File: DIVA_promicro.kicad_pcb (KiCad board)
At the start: 2 copper layers, 65.8 x 91.4 mm, 25 parts

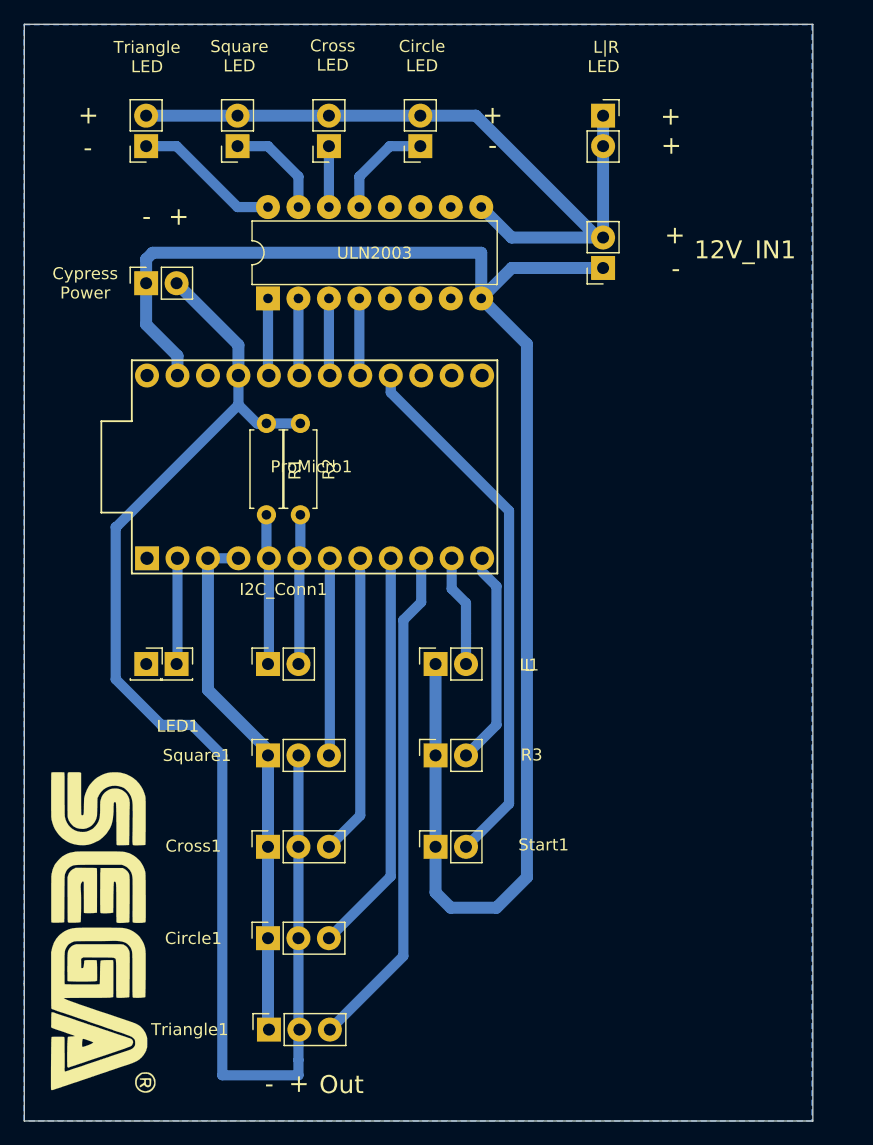
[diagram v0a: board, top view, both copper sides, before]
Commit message: images + visual pcb changes
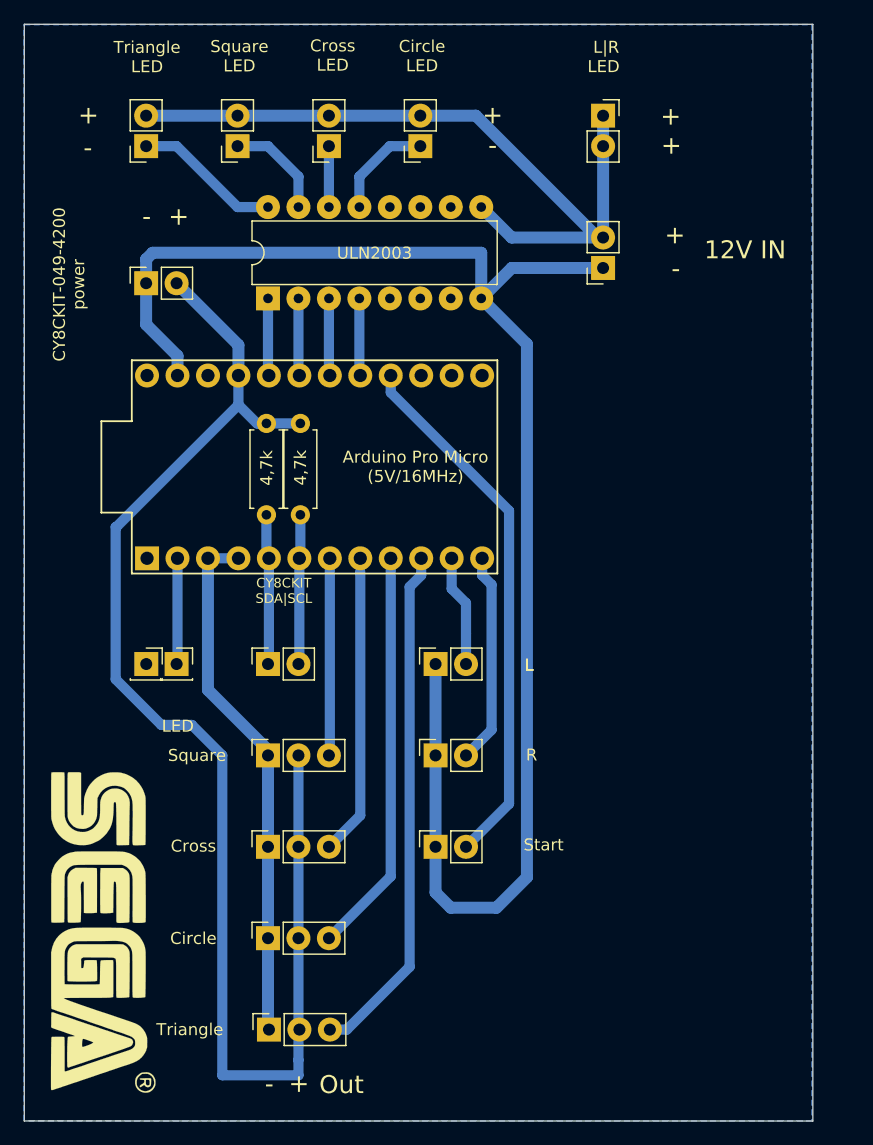
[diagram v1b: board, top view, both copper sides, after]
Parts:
- 12V IN: renamed from 12V_IN1
- CY8CKIT SDA|SCL: renamed from I2C_Conn1
- renumbered R2 to 4,7k, R1 to 4,7k, Circle1 to Circle, Cross1 to Cross, L1 to L, LED1 to LED, R3 to R, Square1 to Square, Start1 to Start, Triangle1 to Triangle
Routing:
- net Net-(J1-Pad3): track 42.4 -> 43.3 mm
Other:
- board text added: "Arduino Pro Micro (5V/16MHz)"
- board text added: "CY8CKIT SCL|SDA"
- board text added: "CY8CKIT SDA|SCL"
- board text added: "CY8CKIT-049-4200 power"
- board text removed: "Cypress Power"
- board text removed: "SCL|SDA"

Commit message: Added mounting holes for a DC/DC step-down modules
Added mounting holes for a DC/DC step-down modules XL4015 (bigger) and LM2596S (smaller) if you will install 5V WS2812B LED strip.  But footprints for them need to be confirmed.
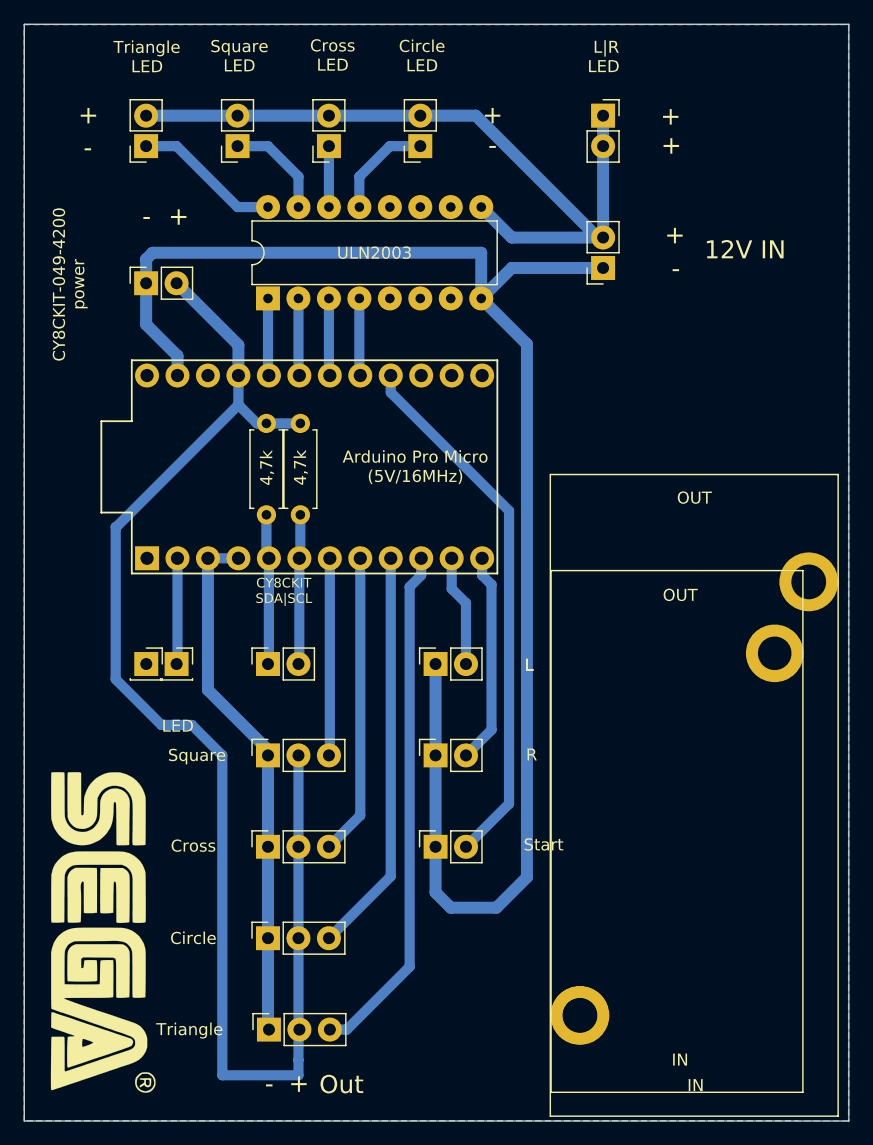
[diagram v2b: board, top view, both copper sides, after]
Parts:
- added REF**: LM2596S_DCDC_converter_smaller, lm2596dcdc:LM2596S_DCDC_converter_smaller, F.Cu at (145.5, 76.0)
- added REF**: XL4015_DCDC_converter_bigger, lm2596dcdc:XL4015_DCDC_converter_bigger, F.Cu at (145.5, 68.0)
- moved G*** 4.86 mm to (153.3, 78.1)
- moved REF** 4.08 mm to (163.4, 39.4)
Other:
- board size 65.8 x 91.4 mm -> 68.8 x 91.4 mm

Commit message: update
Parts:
- moved REF** 58.5 mm to (169.5, 121.3), turned to 180 degrees
- moved REF** 48.1 mm to (166.6, 119.3), turned to 180 degrees

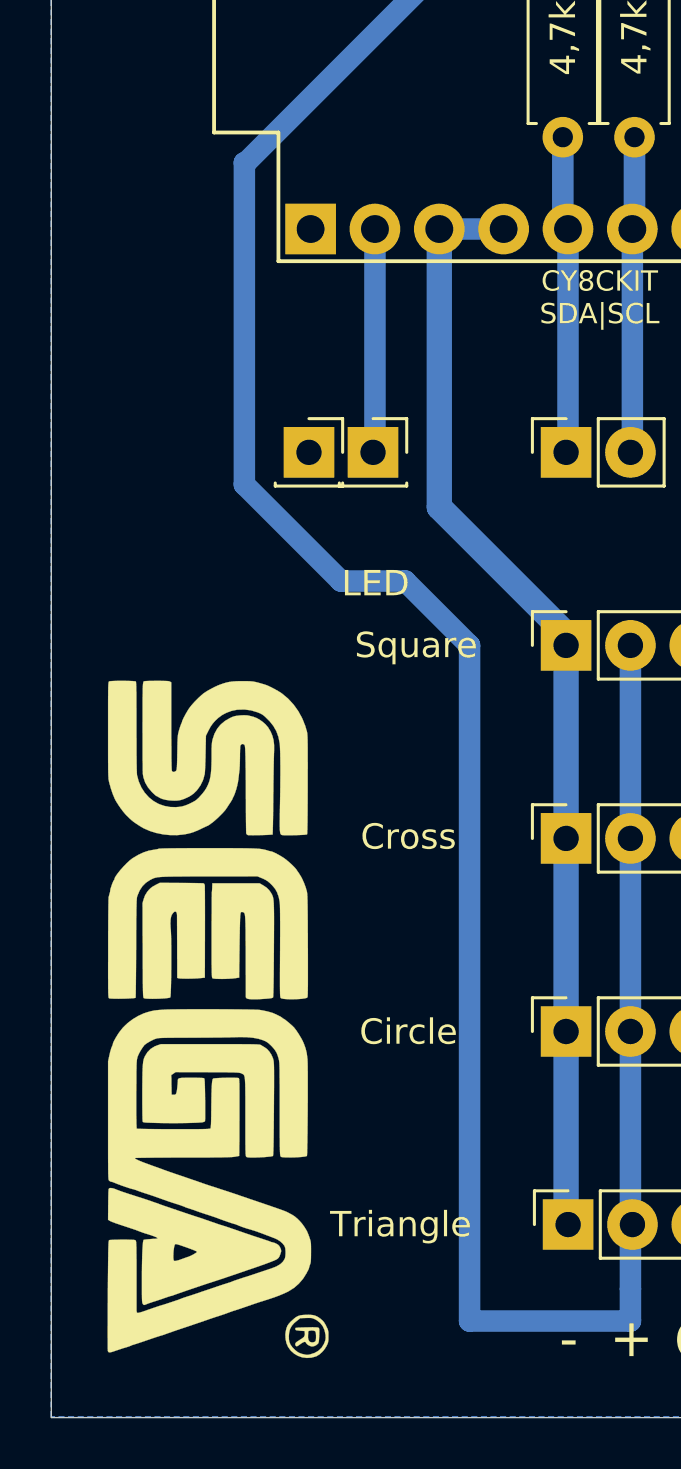
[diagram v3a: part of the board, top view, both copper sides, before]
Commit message: Added resistor for a LED strip signal line
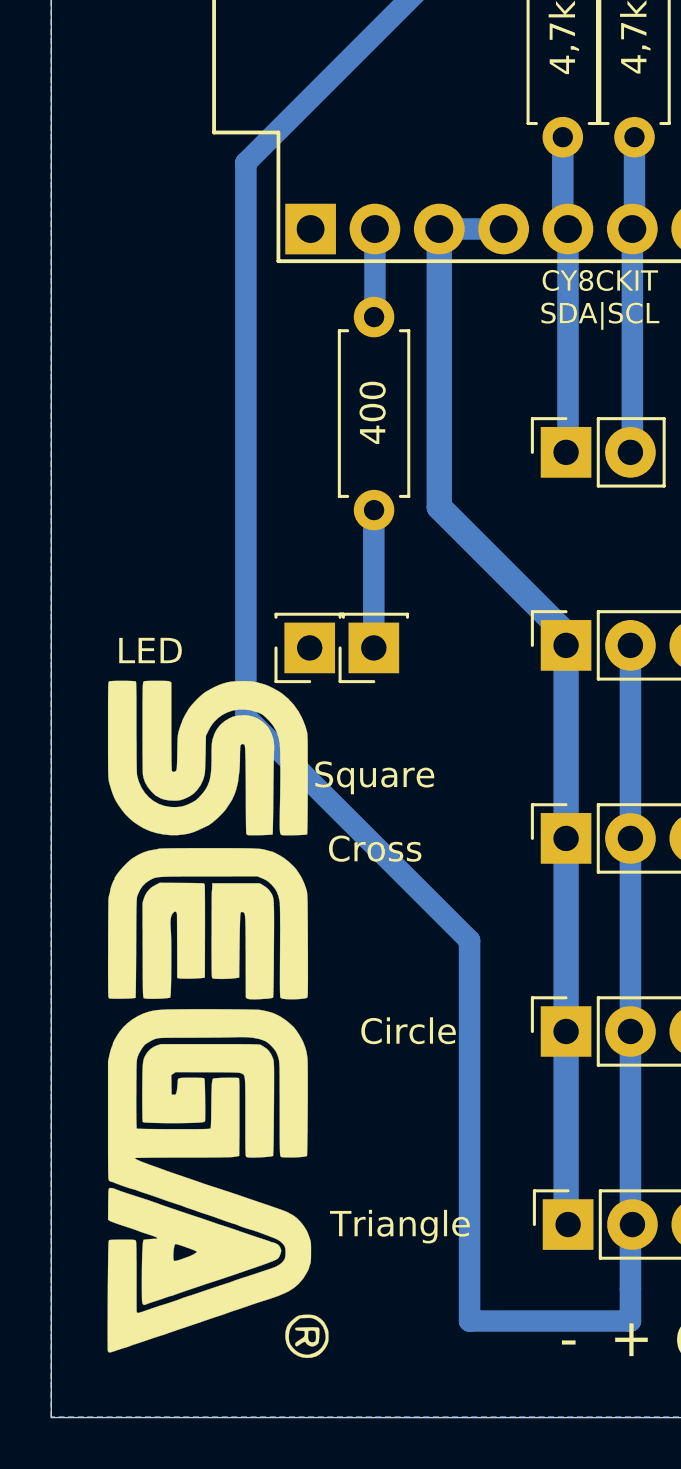
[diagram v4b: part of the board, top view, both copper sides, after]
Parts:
- added 400: 500, Resistor_THT:R_Axial_DIN0207_L6.3mm_D2.5mm_P7.62mm_Horizontal, F.Cu at (114.3, 78.5)
- moved LED1 8.13 mm to (114.3, 91.5), turned to 180 degrees
- moved LED 8.11 mm to (111.8, 91.5), turned to 180 degrees
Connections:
- LED1 pad 1: Net-(J7-Pad1) -> Net-(LED1-Pad1)
- ProMicro1 pad 10: Net-(J1-Pad3) -> Net-(ProMicro1-Pad10)
- ProMicro1 pad 11: Net-(J6-Pad2) -> Net-(L1-Pad2)
- ProMicro1 pad 12: Net-(J4-Pad2) -> Net-(ProMicro1-Pad12)
- ProMicro1 pad 16: Net-(J9-Pad2) -> Net-(ProMicro1-Pad16)
- ProMicro1 pad 2: Net-(J7-Pad1) -> Net-(ProMicro1-Pad2)
- ProMicro1 pad 6: Net-(J8-Pad2) -> Net-(I2C_Conn1-Pad2)
- ProMicro1 pad 7: Net-(J5-Pad3) -> Net-(ProMicro1-Pad7)
- ProMicro1 pad 8: Net-(J3-Pad3) -> Net-(Cross1-Pad3)
- ProMicro1 pad 9: Net-(J2-Pad3) -> Net-(Circle1-Pad3)
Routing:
- net Net-(J7-Pad1): track 8.85 -> 0.00 mm
- net Net-(LED1-Pad1): track 0.00 -> 5.49 mm
- net Net-(ProMicro1-Pad2): track 0.00 -> 3.49 mm
- net Net-(Circle1-Pad2): track 116.9 -> 115.3 mm
